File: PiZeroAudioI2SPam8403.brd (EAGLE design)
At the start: 65.1 x 30.2 mm, 60 parts, among them CON1 RPI-Header, J1 GROVE, J2 2X2HEADER, J3 JST, J4 AMP FCI 10103594-0001LF, J5 2X1-LOCKING, J6 GROVE, J7 4X1-LOCKING, Q1 DMG2305UX, U1 TXB0104PWR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

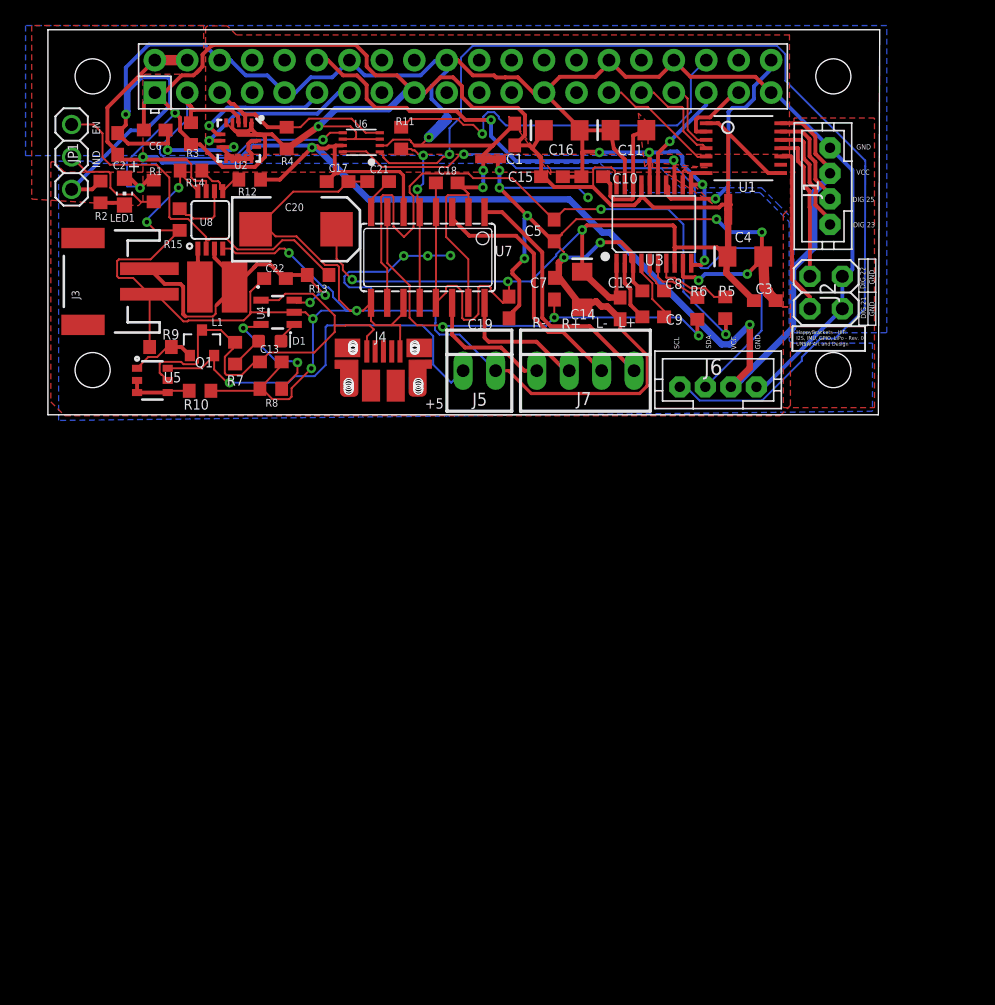
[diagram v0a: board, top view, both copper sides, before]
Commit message: Swapped position of Mosfet Capacitively coupled Audio Set OE of I2C translator to GND Set Mute so it floats to +5
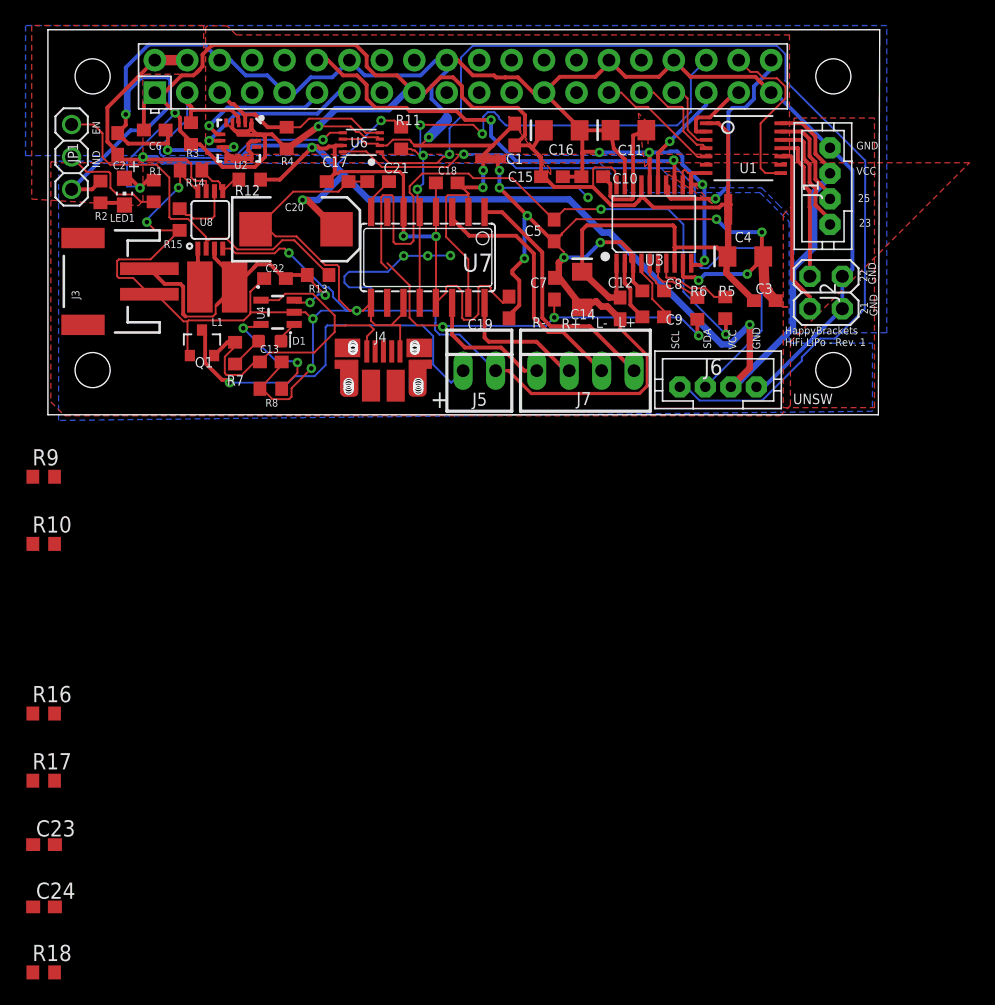
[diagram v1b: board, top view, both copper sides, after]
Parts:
- removed U5: DMMT5401, HappyBrackets:SOT26-TRANS
- added C23, C24: 1uF, rcl:C0603
- added R16, R17: 160K, adafruit:R0603
- added R18: 1K, adafruit:R0603
- L1: value IFSC1515AHER2R2M01 -> 2.2uH
- R10: value 10K -> 180
- R9: value 47K -> 180
- moved R10 17.1 mm to (-79.1, -8.84)
- moved R9 13.7 mm to (-79.1, -3.58), turned to 0 degrees
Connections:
- removed net N$22: R10.1, U5.B1, U5.B2, U5.C2
- removed net N$27: Q1.G, R9.1, U5.C1
- new net N$10: R17.2, U7.10
- new net N$13: C23.1, R16.1
- new net N$8: R16.2, U7.7
- new net OE: CON1.38, U1.8
- net +3V3: no longer U1.8, U6.P$6
- net +5V: now also C18.1, C19.1, C20.+, R11.1, U7.13, U7.4
- net +5V-IN: now also Q1.D; no longer Q1.S, U5.E1
- net +5VCHARGE: now also Q1.S; no longer Q1.D, U5.E2
- net /MUTE: now also R11.2, R18.1, R18.2, U7.12, U7.5; no longer R11.1
- net AGND: now also Q1.G; no longer R10.2, R9.2
- net AN3V3: no longer C18.1, C19.1, C20.+, U7.13, U7.4
- net AUDIO-LEFT: now also C23.2, R9.1; no longer U7.7
- net AUDIO-RIGHT: now also R10.1; no longer U7.10
- net GND: now also C24.2, R10.2, R9.2, U6.P$6
- net N$5: now also C24.1, R17.1; no longer R11.2, U7.12, U7.5
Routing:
- net AN3V3: track 78.9 -> 32.0 mm, vias 3 -> 0
- net +5V: track 128.6 -> 169.0 mm, vias 3 -> 7
- net /MUTE: track 30.4 -> 44.7 mm, vias 1 -> 4
- net N$5: track 13.8 -> 0.00 mm, vias 2 -> 0
- net OE: track 0.00 -> 13.4 mm
- net +5VCHARGE: track 36.6 -> 28.4 mm
- net +3V3: track 135.2 -> 128.4 mm
- net AGND: track 230.6 -> 225.4 mm
- net N$27: track 5.10 -> 0.00 mm
- net N$22: track 5.09 -> 0.00 mm
- net AUDIO-LEFT: track 35.6 -> 31.6 mm
- net GND: track 216.7 -> 219.8 mm
- net +5V-IN: track 32.2 -> 30.7 mm
- net AUDIO-RIGHT: track 52.9 -> 52.0 mm
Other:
- board text added: "+"
- board text added: "21"
- board text added: "22"
- board text added: "23"
- board text added: "25"
- board text added: "HappyBrackets HiFi LiPo - Rev. 1"
- board text added: "UNSW"
- board text removed: "+5"
- board text removed: "DIG 21"
- board text removed: "DIG 22"
- board text removed: "DIG 23"
- board text removed: "DIG 25"
- board text removed: "HappyBrackets - HiFi I2S, IMU, GPIO, LiPo - Rev. 0 UNSW Art and Design"
